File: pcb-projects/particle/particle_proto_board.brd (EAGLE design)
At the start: 33.7 x 27.9 mm, 35 parts, among them IC1 ATTINY20-MMH, IC2 DMC2400V, IC3 DMC2400V, J1 FTS-103-01-L-DV, SW1 T/S-PI SW, SW2 T/S-PI SW, SW3 T/S-PI SW

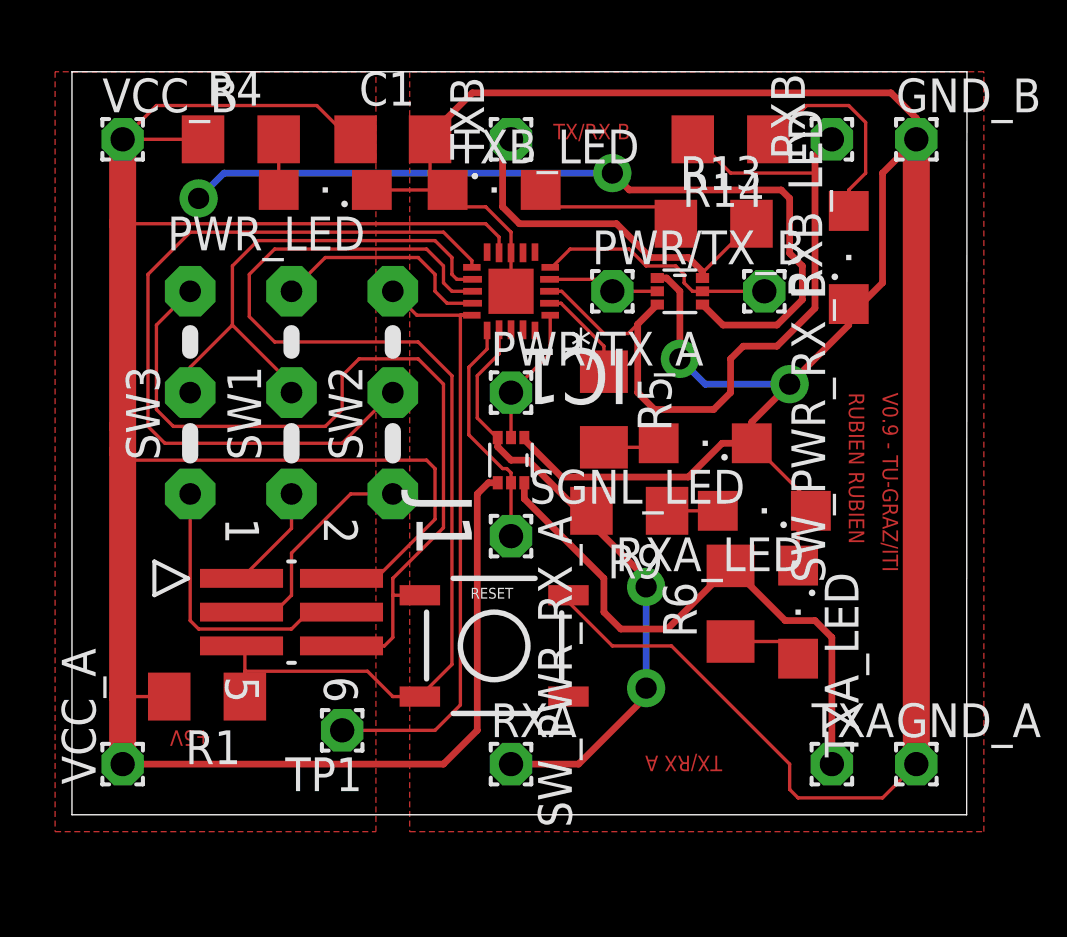
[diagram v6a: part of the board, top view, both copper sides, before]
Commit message: renamed parts in schema
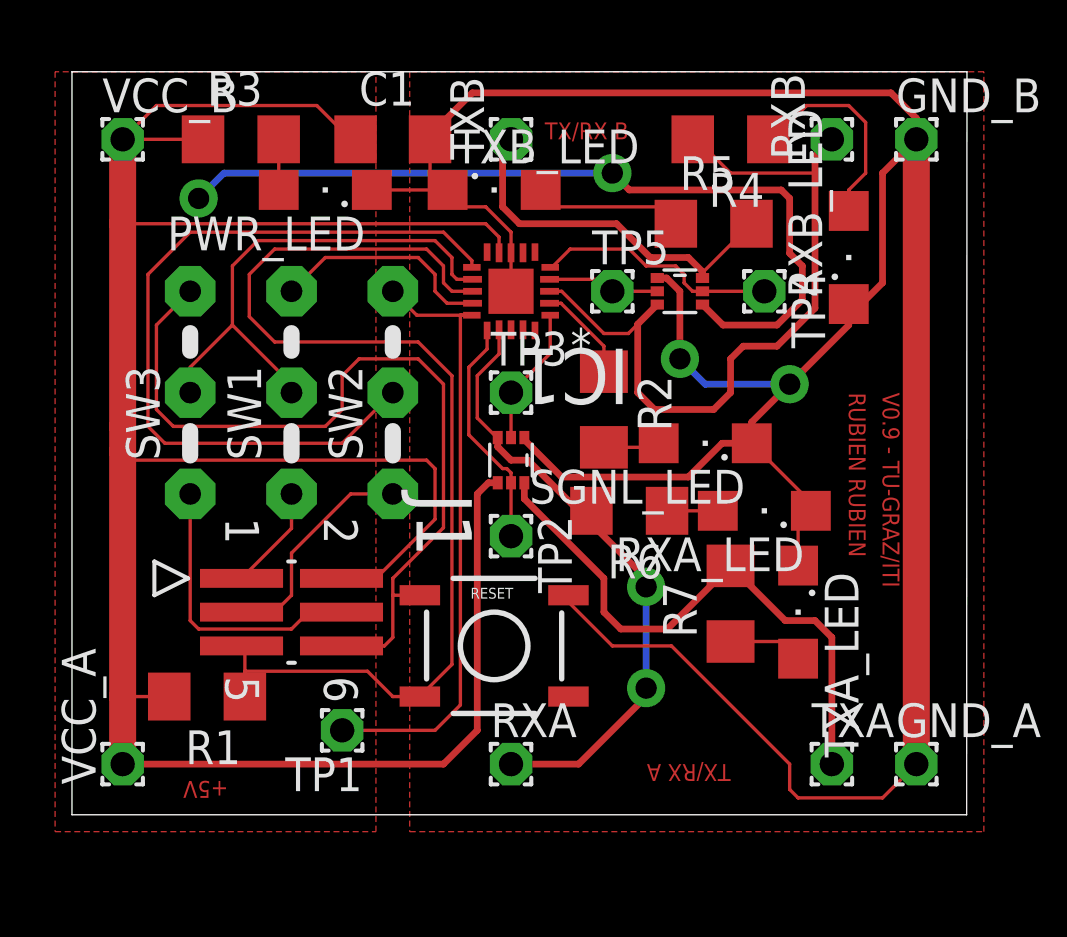
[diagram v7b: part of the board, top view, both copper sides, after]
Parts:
- removed R13, R14, R9: 1k, rcl:R1206
- added R2, R3, R7: 1k, rcl:R1206
- TP2: value SW_PWR_RX_A -> TP2
- TP3: value PWR/TX_A -> TP3
- TP4: value SW_PWR_RX_B -> TP4
- TP5: value PWR/TX_B -> TP5
- moved R4 18.4 mm to (25.4, 25.4), turned to 180 degrees
- moved R5 8.11 mm to (24.8, 22.2), turned to 0 degrees
- moved R6 5.17 mm to (21.6, 11.4), turned to 180 degrees
- renumbered PWR/TX_A to TP3, PWR/TX_B to TP5, SW_PWR_RX_A to TP2, SW_PWR_RX_B to TP4
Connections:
- net N$13: now also R5.1; no longer R13.1
- net N$18: now also R2.2; no longer R5.2
- net N$22: now also R3.2; no longer R4.2
- net N$23: now also R2.1; no longer R5.1
- net N$3: now also R7.1; no longer R6.1
- net N$4: now also R6.1; no longer R9.1
- net N$8: now also R4.1; no longer R14.1
- net RX_A: now also R6.2; no longer R9.2
- net RX_B: now also R4.2; no longer R14.2
- net TX_A: now also R7.2; no longer R6.2
- net TX_B: now also R5.2; no longer R13.2
- net VCC: now also R3.1; no longer R4.1
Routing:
- net GND: track 141.1 -> 141.8 mm

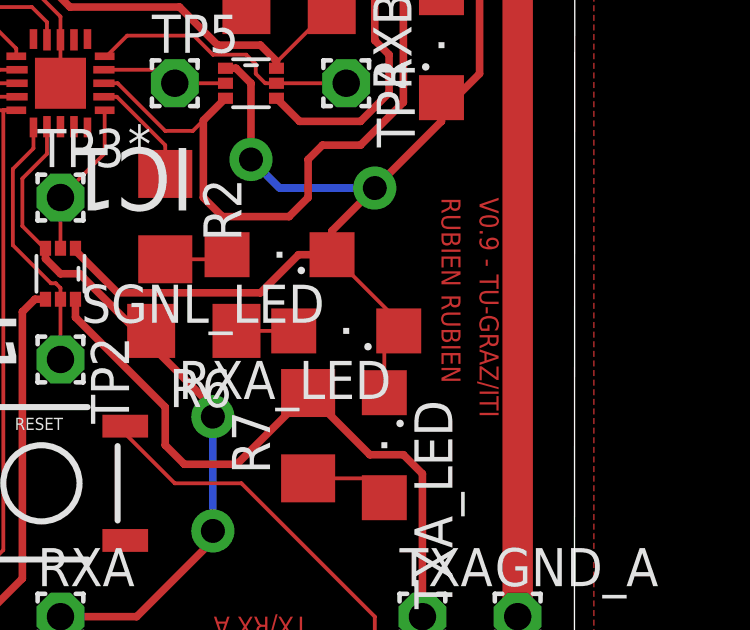
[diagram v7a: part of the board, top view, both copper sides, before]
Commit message: fixed #47
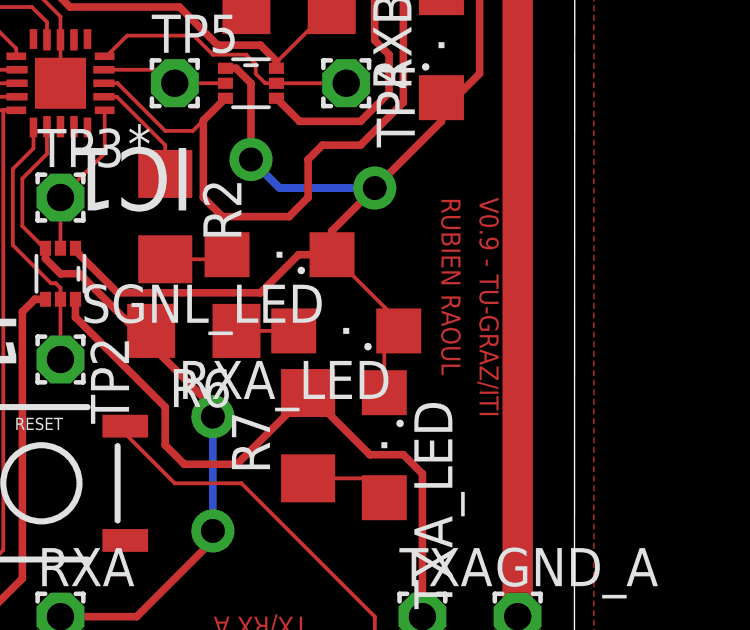
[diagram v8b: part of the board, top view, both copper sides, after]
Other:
- board text added: "RUBIEN RAOUL"
- board text removed: "RUBIEN RUBIEN"
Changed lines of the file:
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@@
 <wire x1="34.29" y1="27.94" x2="0.635" y2="27.94" width="0" layer="20"/>
 <wire x1="0.635" y1="27.94" x2="0.635" y2="0" width="0" layer="20"/>
-<text x="29.845" y="15.875" size="0.635" layer="1" font="vector" ratio="23" distance="8" rot="SR270">RUBIEN RUBIEN</text>
+<text x="29.845" y="15.875" size="0.635" layer="1" font="vector" ratio="23" distance="8" rot="SR270">RUBIEN RAOUL</text>
 <text x="6.50875" y="1.27" size="0.635" layer="1" font="vector" ratio="20" distance="8" rot="SR180">+5V</text>
 <text x="18.415" y="25.4" size="0.635" layer="1" font="vector" ratio="20" distance="8" rot="SR0">TX/RX B</text>
@@
 <wire x1="2.54" y1="25.4" x2="2.54" y2="1.905" width="1.016" layer="29"/>
 <text x="31.115" y="15.875" size="0.635" layer="29" font="vector" ratio="23" distance="8" rot="SR270">V0.9 - TU-GRAZ/ITI</text>
-<text x="29.845" y="15.875" size="0.635" layer="29" font="vector" ratio="23" distance="8" rot="SR270">RUBIEN RUBIEN</text>
+<text x="29.845" y="15.875" size="0.635" layer="29" font="vector" ratio="23" distance="8" rot="SR270">RUBIEN RAOUL</text>
 <text x="25.4" y="1.905" size="0.635" layer="29" font="vector" ratio="20" distance="8" rot="SR180">TX/RX A</text>
 <text x="6.50875" y="1.27" size="0.635" layer="29" font="vector" ratio="20" distance="0" rot="SR180">+5V</text>
@@
 <wire x1="2.8575" y1="14.2875" x2="2.54" y2="14.605" width="0.127" layer="1"/>
 <wire x1="2.8575" y1="13.335" x2="2.54" y2="13.6525" width="0.127" layer="1"/>
+<wire x1="5.563" y1="25.4" x2="6.35" y2="24.13" width="0" layer="19" extent="1-16"/>
 </signal>
 <signal name="TX_B">
